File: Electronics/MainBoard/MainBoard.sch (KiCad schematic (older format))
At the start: 29 parts, among them CN1 RCable_Con_Front, CN2 RCable_Con_Front, CN3 RCable_Con_VEST, J1 CONN_02X04, M1 Vibr_Motor, Q1 Q_PNP_CBE, SW1 SW_PUSH, SW2 SPST

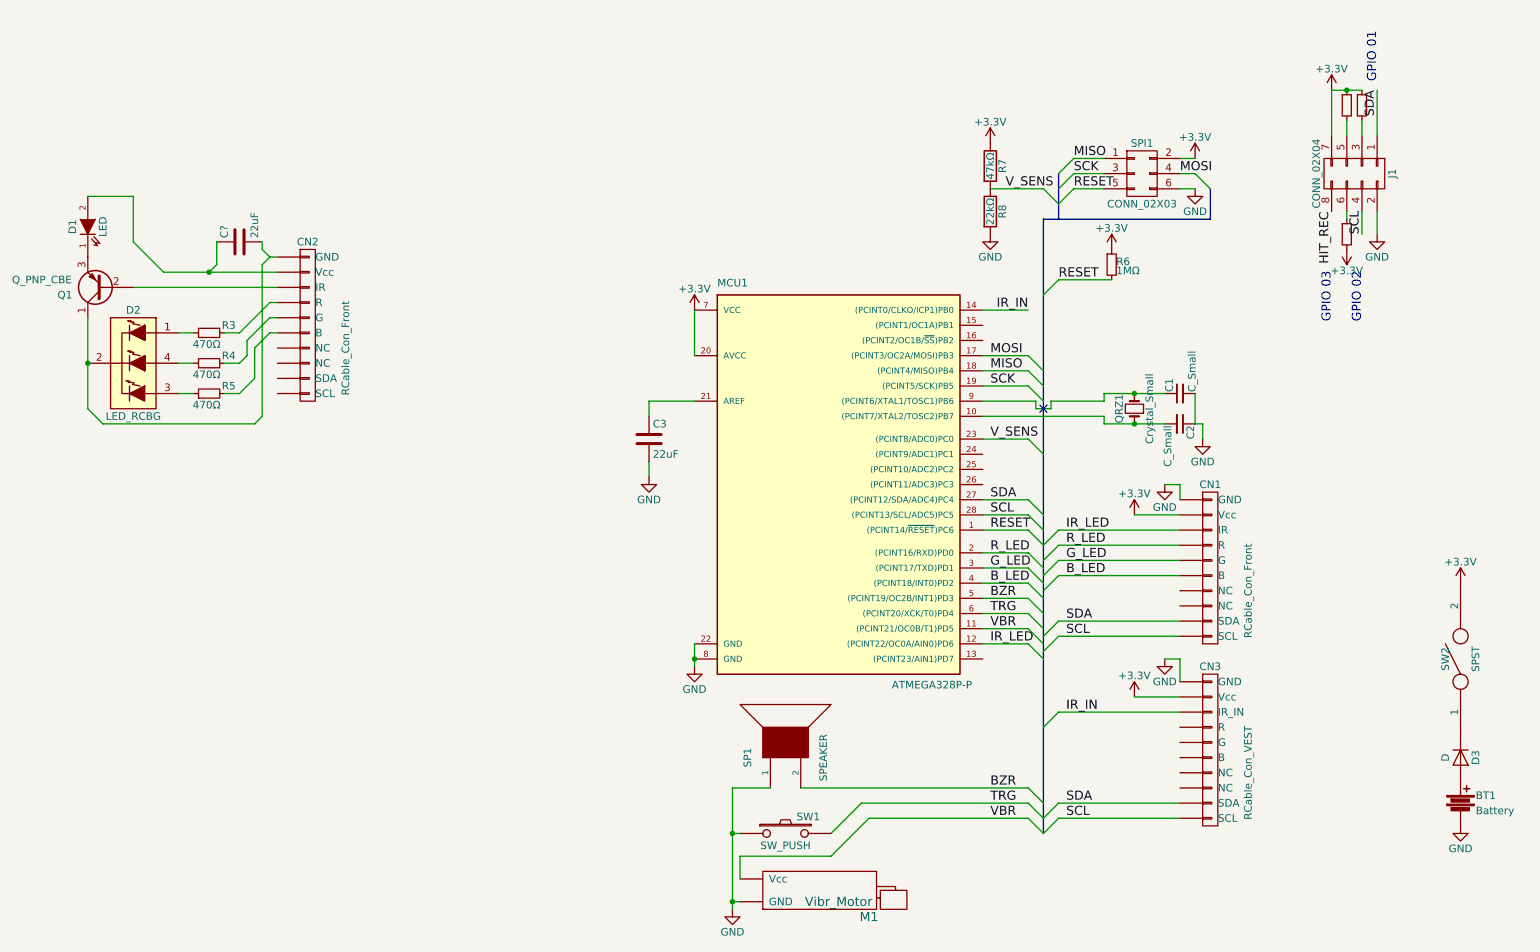
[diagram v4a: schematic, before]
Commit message: Initial modifications. Moved RGB-Muzzle for RX/TX lines, fixed front muzzle LEDs
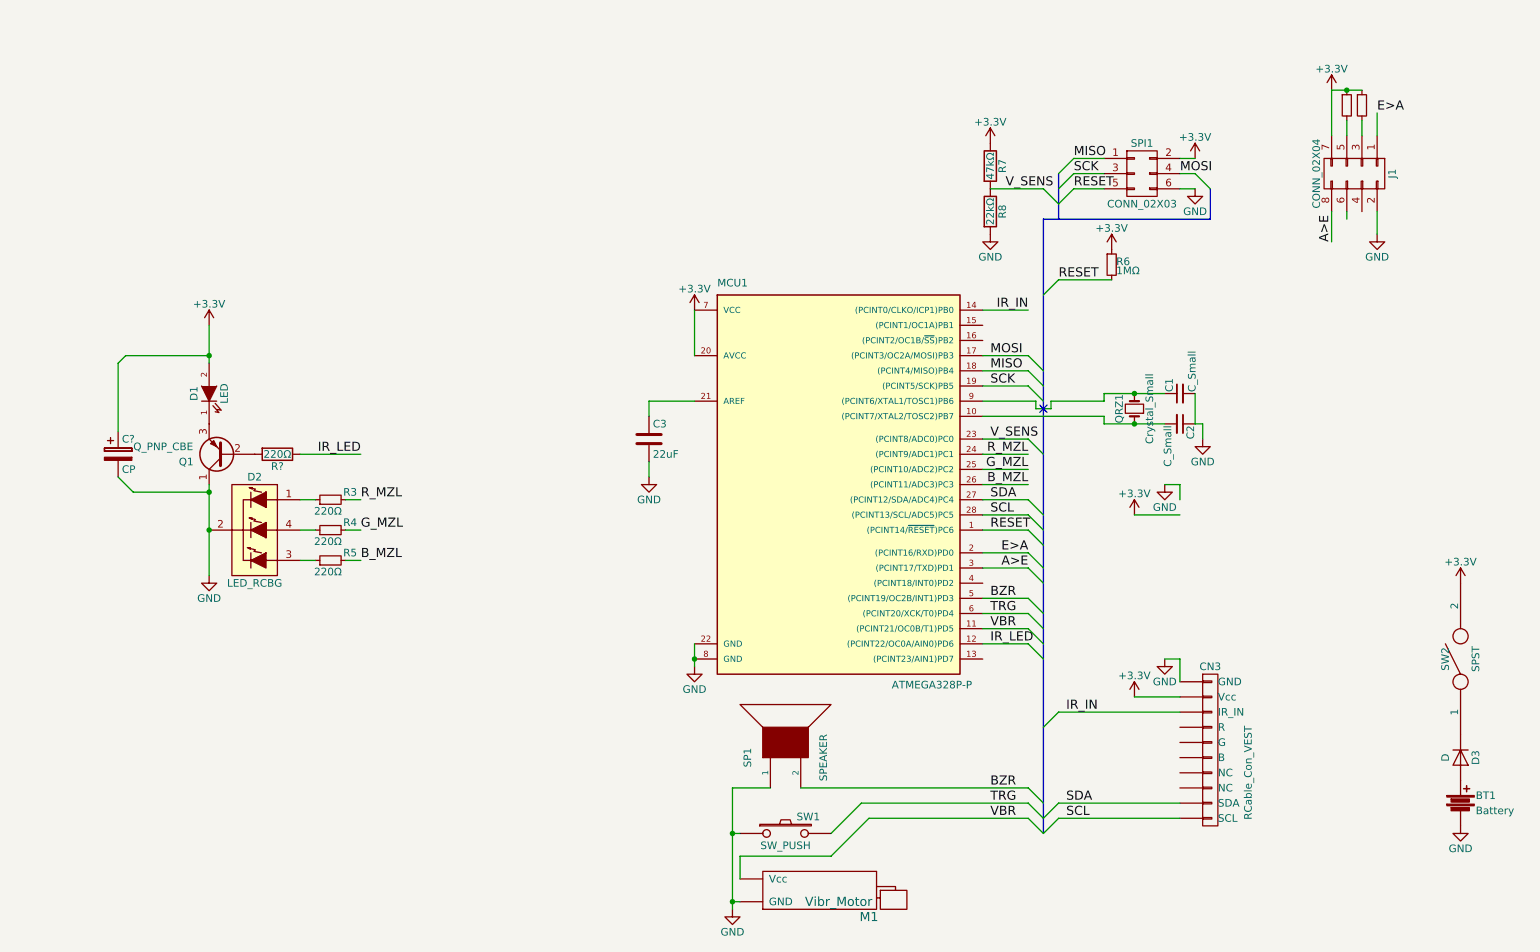
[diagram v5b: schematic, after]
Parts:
- removed C?: 22uF, symbol C
- removed CN1, CN2: RCable_Con_Front, Pin_Headers:Pin_Header_Straight_2x05, symbol RCable_Con_Front
- removed R10: RST, Resistors_ThroughHole:R_Axial_DIN0204_L3.6mm_D1.6mm_P2.54mm_Vertical, symbol R_Small
- added C?: CP, symbol CP
- added R?: 220Ω, symbol R
- R3, R4, R5: value 470Ω -> 220Ω
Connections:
- net HIT_REC is gone; now on net A>E: J1.8 (P8)
- net +3V3: now also D1.2 (A), C?.1
- net GND: now also D2.2 (COMMON_CATHODE), Q1.1 (C), C?.2
- net IR_LED: now also R?.1
- net SCL: no longer J1.4 (P4)
- net SDA: no longer J1.1 (P1)
- net R_MZL: now reaches MCU1.24 ((PCINT9/ADC1)PC1)
- net R_MZL: now also R3.2
- net G_MZL: now reaches MCU1.25 ((PCINT10/ADC2)PC2)
- net G_MZL: now also R4.2
- net B_MZL: now reaches MCU1.26 ((PCINT11/ADC3)PC3)
- net B_MZL: now also R5.2
- net at Q1.2 (B): now also R?.2
- net B_LED: no longer names the net of MCU1.4 ((PCINT18/INT0)PD2)
- net G_LED renamed A>E
- net R_LED renamed E>A
- net E>A: now also J1.1 (P1)
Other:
- note removed: "GPIO 01"
- note removed: "GPIO 02"
- note removed: "GPIO 03"
- moved on the sheet: D1, D2, Q1, R3, R4, R5

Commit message: Small cleanup of schematic & footprint
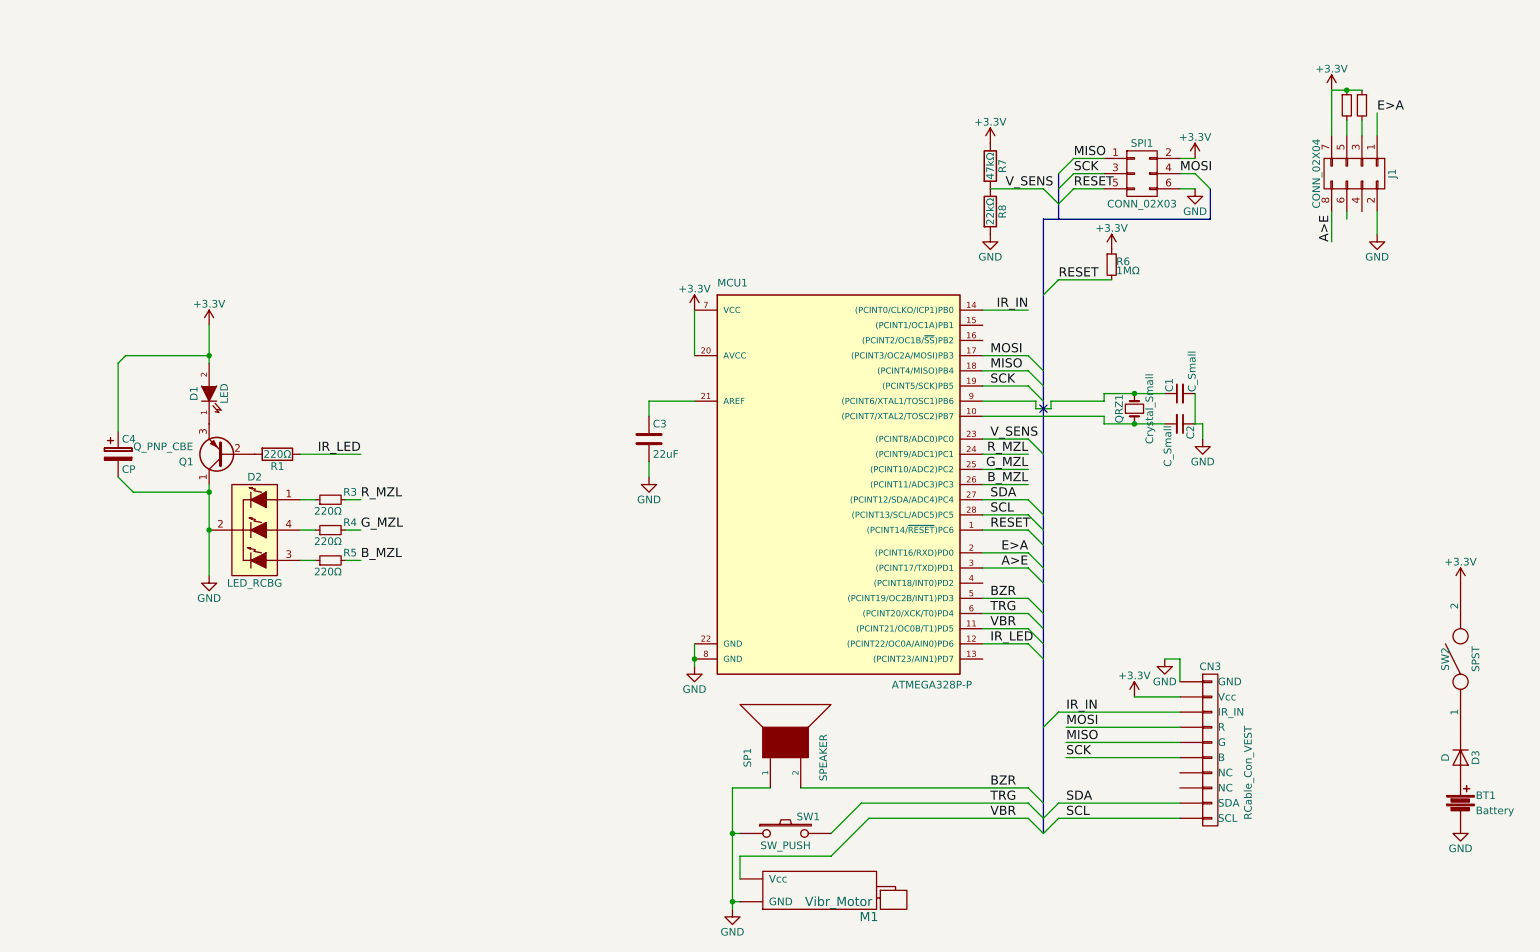
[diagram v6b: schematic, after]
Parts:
- gave numbers to parts that had none: 2
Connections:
- net MISO: now also CN3.5 (G)
- net MOSI: now also CN3.4 (R)
- net SCK: now also CN3.6 (B)
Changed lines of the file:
@@
 EESchema Schematic File Version 2
-LIBS:MainBoard-rescue
 LIBS:power
 LIBS:device
@@
 $EndComp
 Wire Wire Line
-	7900 3200 8100 3200
-Wire Wire Line
-	8100 3200 8300 3200
-Wire Wire Line
-	7900 3000 8100 3000
-Wire Wire Line
-	8100 3000 8300 3000
+	7900 3200 8300 3200
+Wire Wire Line
+	7900 3000 8300 3000
 Wire Wire Line
 	8500 3000 8500 3200
@@
 $EndComp
 Wire Wire Line
-	5200 4650 5200 4750
-Wire Wire Line
-	5200 4750 5200 4800
+	5200 4650 5200 4800
 Connection ~ 5200 4750
 Wire Wire Line
@@
 $EndComp
 Wire Bus Line
-	7500 1850 7500 2350
-Wire Bus Line
-	7500 2350 7500 2850
-Wire Bus Line
-	7500 2850 7500 2950
-Wire Bus Line
-	7500 2950 7500 3050
-Wire Bus Line
-	7500 3050 7500 3400
-Wire Bus Line
-	7500 3400 7500 3800
-Wire Bus Line
-	7500 3800 7500 3900
-Wire Bus Line
-	7500 3900 7500 4000
-Wire Bus Line
-	7500 4000 7500 4150
-Wire Bus Line
-	7500 4150 7500 4250
-Wire Bus Line
-	7500 4250 7500 4350
-Wire Bus Line
-	7500 4350 7500 4450
-Wire Bus Line
-	7500 4450 7500 4550
-Wire Bus Line
-	7500 4550 7500 4650
-Wire Bus Line
-	7500 4650 7500 4750
-Wire Bus Line
-	7500 4750 7500 5200
-Wire Bus Line
-	7500 5200 7500 5700
-Wire Bus Line
-	7500 5700 7500 5800
-Wire Bus Line
-	7500 5800 7500 5900
+	7500 1850 7500 5900
 Wire Wire Line
 	7900 1450 7700 1450
@@
 	8500 1550 8600 1650
 Wire Bus Line
-	7600 1550 7600 1650
-Wire Bus Line
-	7600 1650 7600 1750
-Wire Bus Line
-	7600 1750 7600 1850
+	7600 1550 7600 1850
 Wire Bus Line
 	8600 1850 7500 1850
@@
 $EndComp
 Wire Wire Line
-	2000 3600 2000 3650
-Wire Wire Line
-	2000 3650 2000 3900
-Wire Wire Line
-	2000 3900 2000 4200
+	2000 3600 2000 4200
 Connection ~ 2000 3900
 $Comp
@@
 	2600 4100 2700 4100
 $Comp
-L GND #PWR07
-U 1 1 572D7F60
-P 8300 3600
-F 0 "#PWR07" H 8300 3350 50  0001 C CNN
-F 1 "GND" H 8300 3450 50  0000 C CNN
-F 2 "" H 8300 3600 50  0000 C CNN
-F 3 "" H 8300 3600 50  0000 C CNN
-	1    8300 3600
-	1    0    0    -1
-$EndComp
-Wire Wire Line
-	8400 3700 8400 3600
-Wire Wire Line
-	8400 3600 8300 3600
-$Comp
-L +3.3V #PWR08
-U 1 1 572D9157
-P 8100 3800
-F 0 "#PWR08" H 8100 3650 50  0001 C CNN
-F 1 "+3.3V" H 8100 3940 50  0000 C CNN
-F 2 "" H 8100 3800 50  0000 C CNN
-F 3 "" H 8100 3800 50  0000 C CNN
-	1    8100 3800
-	1    0    0    -1
-$EndComp
-Wire Wire Line
-	8100 3800 8400 3800
-$Comp
 L R_Small R6
 U 1 1 572DCB6A
@@
 $EndComp
 $Comp
-L +3.3V #PWR09
+L +3.3V #PWR07
 U 1 1 572DCEA7
 P 7950 2050
-F 0 "#PWR09" H 7950 1900 50  0001 C CNN
+F 0 "#PWR07" H 7950 1900 50  0001 C CNN
 F 1 "+3.3V" H 7950 2190 50  0000 C CNN
 F 2 "" H 7950 2050 50  0000 C CNN
@@
 $EndComp
 $Comp
-L GND #PWR010
+L GND #PWR08
 U 1 1 572CF9FB
 P 7150 1950
-F 0 "#PWR010" H 7150 1700 50  0001 C CNN
+F 0 "#PWR08" H 7150 1700 50  0001 C CNN
 F 1 "GND" H 7150 1800 50  0000 C CNN
 F 2 "" H 7150 1950 50  0000 C CNN
@@
 $EndComp
 $Comp
-L +3.3V #PWR011
+L +3.3V #PWR09
 U 1 1 572CFBB3
 P 7150 1350
-F 0 "#PWR011" H 7150 1200 50  0001 C CNN
+F 0 "#PWR09" H 7150 1200 50  0001 C CNN
 F 1 "+3.3V" H 7150 1490 50  0000 C CNN
 F 2 "" H 7150 1350 50  0000 C CNN
@@
 SCL
 $Comp
-L GND #PWR012
+L GND #PWR010
 U 1 1 572D931B
 P 8300 4750
-F 0 "#PWR012" H 8300 4500 50  0001 C CNN
+F 0 "#PWR010" H 8300 4500 50  0001 C CNN
 F 1 "GND" H 8300 4600 50  0000 C CNN
 F 2 "" H 8300 4750 50  0000 C CNN
@@
 	8400 4750 8300 4750
 $Comp
-L +3.3V #PWR013
+L +3.3V #PWR011
 U 1 1 572D98DD
 P 8100 5000
-F 0 "#PWR013" H 8100 4850 50  0001 C CNN
+F 0 "#PWR011" H 8100 4850 50  0001 C CNN
 F 1 "+3.3V" H 8100 5140 50  0000 C CNN
 F 2 "" H 8100 5000 50  0000 C CNN
@@
 	5700 5600 5450 5600
 Wire Wire Line
-	5450 5600 5450 5900
-Wire Wire Line
-	5450 5900 5450 6350
-Wire Wire Line
-	5450 6350 5450 6400
+	5450 5600 5450 6400
 Wire Wire Line
 	5450 5900 5500 5900
@@
 Connection ~ 5450 6350
 $Comp
-L GND #PWR014
+L GND #PWR012
 U 1 1 572E5080
 P 5450 6400
-F 0 "#PWR014" H 5450 6150 50  0001 C CNN
+F 0 "#PWR012" H 5450 6150 50  0001 C CNN
 F 1 "GND" H 5450 6250 50  0000 C CNN
 F 2 "" H 5450 6400 50  0000 C CNN
@@
 VBR
 $Comp
-L GND #PWR015
+L GND #PWR013
 U 1 1 572EF82E
 P 8500 1650
-F 0 "#PWR015" H 8500 1400 50  0001 C CNN
+F 0 "#PWR013" H 8500 1400 50  0001 C CNN
 F 1 "GND" H 8500 1500 50  0000 C CNN
 F 2 "" H 8500 1650 50  0000 C CNN
@@
 	9700 1800 9700 1950
 $Comp
-L +3.3V #PWR016
+L +3.3V #PWR014
 U 1 1 595AF7EE
 P 9400 1000
-F 0 "#PWR016" H 9400 850 50  0001 C CNN
+F 0 "#PWR014" H 9400 850 50  0001 C CNN
 F 1 "+3.3V" H 9400 1140 50  0000 C CNN
 F 2 "" H 9400 1000 50  0001 C CNN
@@
 $EndComp
 Wire Wire Line
-	9400 1000 9500 1000
-Wire Wire Line
-	9500 1000 9600 1000
-$Comp
-L GND #PWR017
+	9400 1000 9600 1000
+$Comp
+L GND #PWR015
 U 1 1 595B47CF
 P 9700 1950
-F 0 "#PWR017" H 9700 1700 50  0001 C CNN
+F 0 "#PWR015" H 9700 1700 50  0001 C CNN
 F 1 "GND" H 9700 1800 50  0000 C CNN
 F 2 "" H 9700 1950 50  0001 C CNN
@@
 	4900 3450 4900 3550
 $Comp
-L GND #PWR019
+L GND #PWR016
 U 1 1 595C115B
 P 4900 3550
-F 0 "#PWR019" H 4900 3300 50  0001 C CNN
+F 0 "#PWR016" H 4900 3300 50  0001 C CNN
 F 1 "GND" H 4900 3400 50  0000 C CNN
 F 2 "" H 4900 3550 50  0001 C CNN
@@
 E>A
 Wire Wire Line
-	2000 2800 2000 2750
-Wire Wire Line
-	2000 2750 2000 2550
-$Comp
-L +3.3V #PWR?
+	2000 2550 2000 2800
+$Comp
+L +3.3V #PWR017
 U 1 1 596FE8E8
 P 2000 2550
-F 0 "#PWR?" H 2000 2400 50  0001 C CNN
+F 0 "#PWR017" H 2000 2400 50  0001 C CNN
 F 1 "+3.3V" H 2000 2690 50  0000 C CNN
 F 2 "" H 2000 2550 50  0001 C CNN
@@
 $EndComp
 $Comp
-L CP C?
+L CP C4
 U 1 1 596FED2A
 P 1400 3400
-F 0 "C?" H 1425 3500 50  0000 L CNN
+F 0 "C4" H 1425 3500 50  0000 L CNN
 F 1 "CP" H 1425 3300 50  0000 L CNN
 F 2 "" H 1438 3250 50  0001 C CNN
@@
 Connection ~ 2000 3650
 $Comp
-L GND #PWR?
+L GND #PWR018
 U 1 1 59700916
 P 2000 4200
-F 0 "#PWR?" H 2000 3950 50  0001 C CNN
+F 0 "#PWR018" H 2000 3950 50  0001 C CNN
 F 1 "GND" H 2000 4050 50  0000 C CNN
 F 2 "" H 2000 4200 50  0001 C CNN
@@
 $EndComp
 $Comp
-L R R?
+L R R1
 U 1 1 59700C12
 P 2450 3400
-F 0 "R?" V 2530 3400 50  0000 C CNN
+F 0 "R1" V 2530 3400 50  0000 C CNN
 F 1 "220Ω" V 2450 3400 50  0000 C CNN
 F 2 "" V 2380 3400 50  0001 C CNN
@@
 Text Label 9700 1150 0    60   ~ 0
 E>A
+Wire Wire Line
+	8400 5200 7650 5200
+Text Label 7650 5200 0    60   ~ 0
+MOSI
+Text Label 7650 5300 0    60   ~ 0
+MISO
+Text Label 7650 5400 0    60   ~ 0
+SCK
+Wire Wire Line
+	8400 5300 7650 5300
+Wire Wire Line
+	8400 5400 7650 5400
 $EndSCHEMATC

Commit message: Associated Footprints
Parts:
- C4: footprint (none) -> Capacitors_ThroughHole:CP_Radial_D4.0mm_P2.00mm
- R1: footprint (none) -> Resistors_ThroughHole:R_Axial_DIN0204_L3.6mm_D1.6mm_P2.54mm_Vertical
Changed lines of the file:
@@
 EESchema Schematic File Version 2
+LIBS:MainBoard-rescue
 LIBS:power
 LIBS:device
@@
 F 0 "C4" H 1425 3500 50  0000 L CNN
 F 1 "CP" H 1425 3300 50  0000 L CNN
-F 2 "" H 1438 3250 50  0001 C CNN
+F 2 "Capacitors_ThroughHole:CP_Radial_D4.0mm_P2.00mm" H 1438 3250 50  0001 C CNN
 F 3 "" H 1400 3400 50  0001 C CNN
 	1    1400 3400
@@
 F 0 "R1" V 2530 3400 50  0000 C CNN
 F 1 "220Ω" V 2450 3400 50  0000 C CNN
-F 2 "" V 2380 3400 50  0001 C CNN
+F 2 "Resistors_ThroughHole:R_Axial_DIN0204_L3.6mm_D1.6mm_P2.54mm_Vertical" V 2380 3400 50  0001 C CNN
 F 3 "" H 2450 3400 50  0001 C CNN
 	1    2450 3400
